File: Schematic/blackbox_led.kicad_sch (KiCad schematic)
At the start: 26 parts, among them U10 CSNP1GCR01-BOW

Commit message: reviewing and refactoring footprints and full schematic
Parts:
- C45: MPN (none) -> 0603B104K500NT; Manufacturer (none) -> FH
- C46: MPN (none) -> CC0603KRX7R9BB103; Manufacturer (none) -> YAGEO
- D10, D11, D12, D13, D3, D4, D5, D6, D7, D8, D9: MPN (none) -> NCD0603R3; Manufacturer (none) -> NATIONSTAR
- R28, R29, R30: MPN (none) -> 0603WAF4700T5E; Manufacturer (none) -> UNI-ROYAL
- R31, R32, R33, R34: MPN (none) -> RC0603FR-071KL; Manufacturer (none) -> YAGEO
- R35, R36, R37, R38, R39: MPN (none) -> 0603WAF1002T5E; Manufacturer (none) -> UNI-ROYAL
- U10: MPN (none) -> CSNP1GCR01-BOW; Manufacturer (none) -> CS Semiconductor

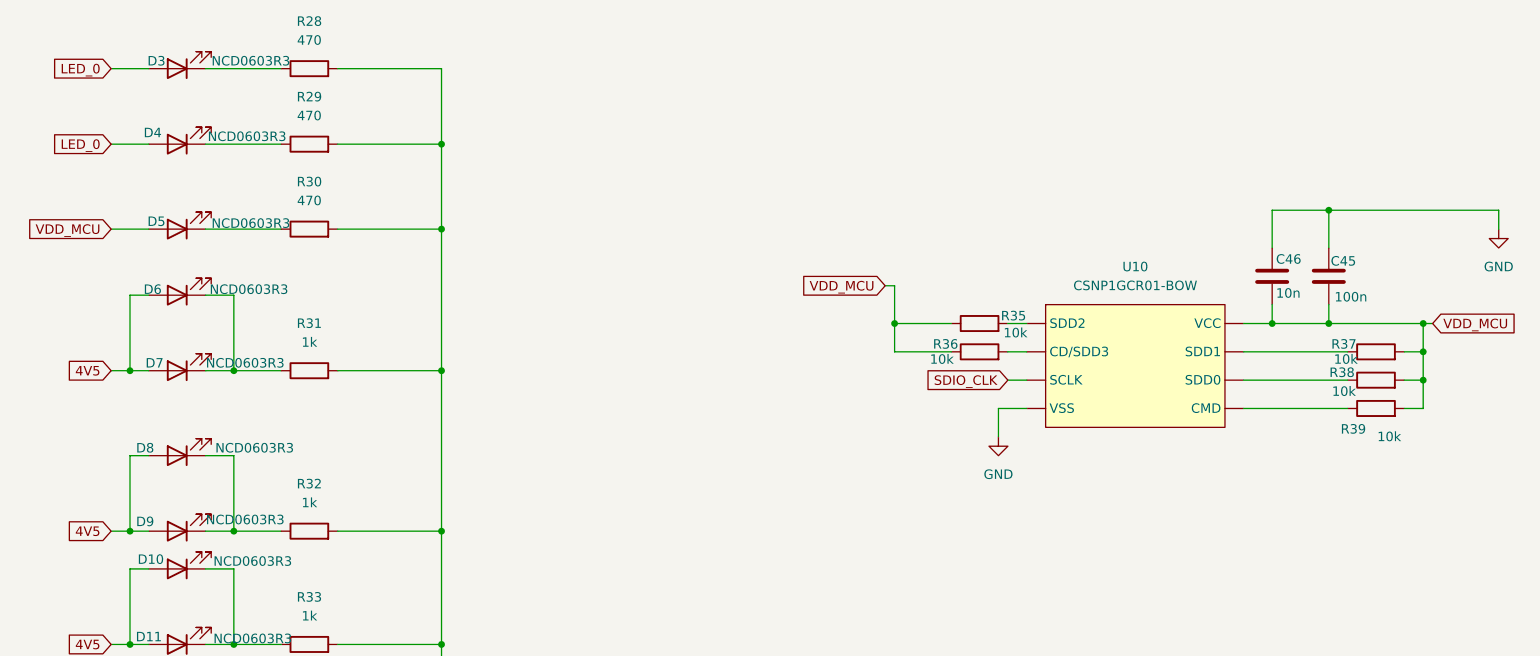
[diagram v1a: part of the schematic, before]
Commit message: Refactor fp-lib-table: Remove unused libraries and update description for fch7_fp
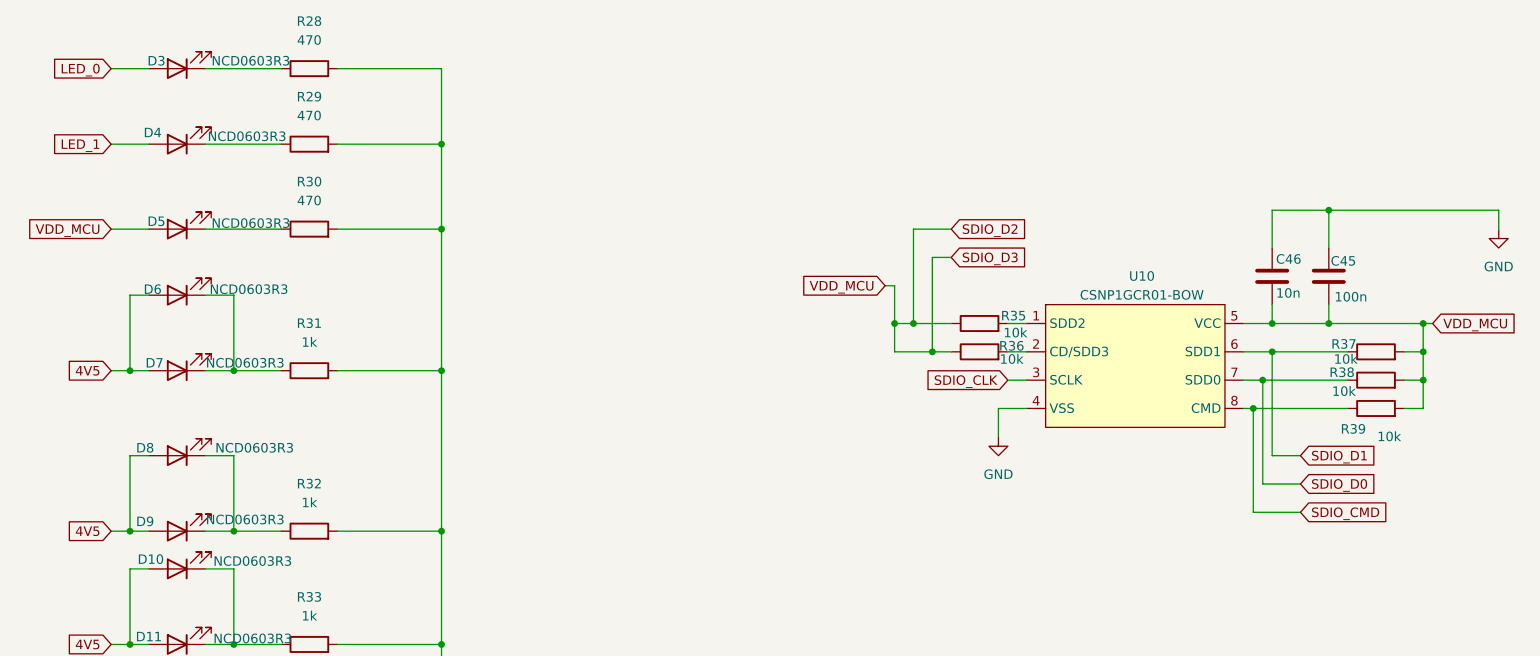
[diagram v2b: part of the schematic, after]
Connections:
- net GND: now also U10.4 (VSS); no longer U10. (CMD)
- net LED_0: no longer D4.2 (A)
- net SDIO_CLK: now also U10.3 (SCLK); no longer U10. (CMD)
- net SDIO_D0: now reaches R38.1
- net SDIO_D0: now also U10.7 (SDD0); no longer U10. (CMD)
- net SDIO_D1: now reaches R37.1
- net SDIO_D1: now also U10.6 (SDD1); no longer U10. (CMD)
- net at R35.2: now also U10.1 (SDD2); no longer U10. (CMD)
- net at R36.2: now also U10.2 (CD/SDD3); no longer U10. (CMD)
- net SDIO_CMD: now reaches R39.1
- net SDIO_CMD: now also U10.8 (CMD); no longer U10. (CMD)
- net VDD_MCU renamed SDIO_D2
- net SDIO_D2: now also U10.5 (VCC); no longer U10. (CMD)
- new net LED_1: D4.2 (A)

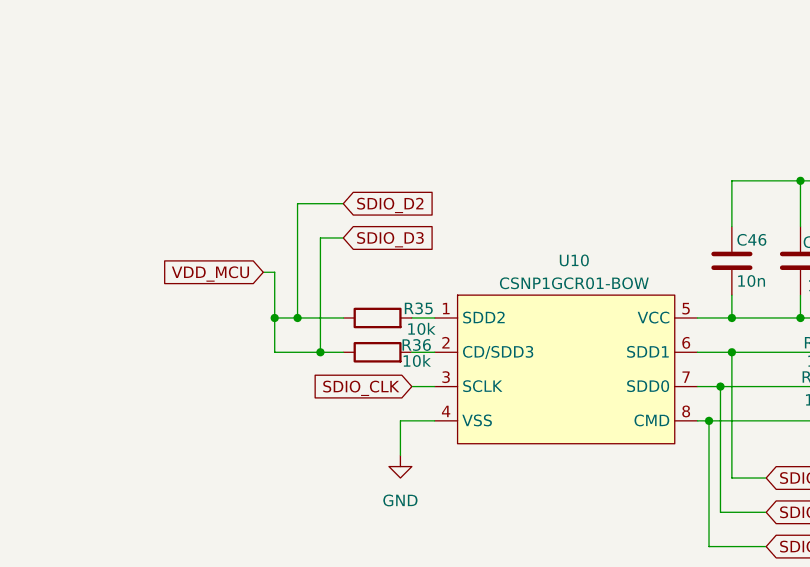
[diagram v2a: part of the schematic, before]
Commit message: Refactor schematic files and update component placements
- Adjusted component positions in osd.kicad_sch for better layout.
- Added new junctions and wires in rf_rx.kicad_sch to improve connectivity.
- Introduced additional junctions and wires in sensors.kicad_sch for enhanced signal routing.
- Removed outdated backup file fch7-2025-11-18_191836.zip and added new backup fch7-2025-11-27_202230.zip.
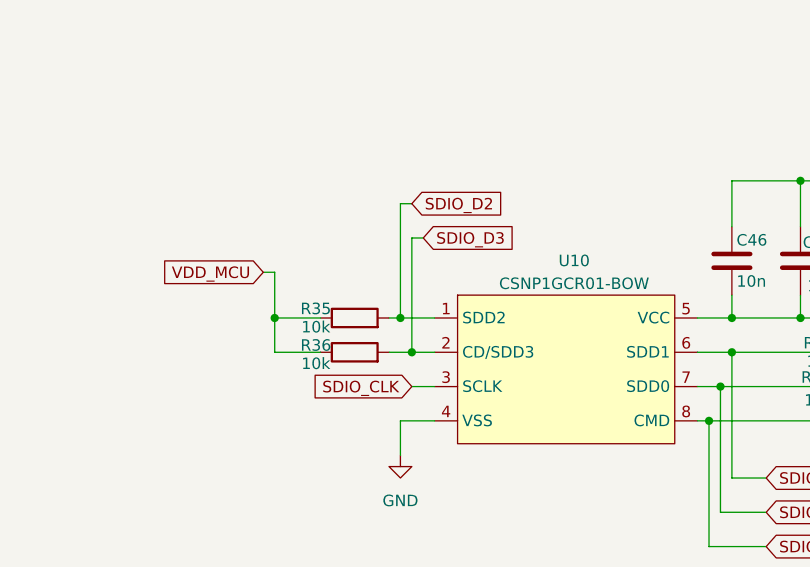
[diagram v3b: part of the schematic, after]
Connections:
- net SDIO_D2: now also R35.2, U10.1 (SDD2); no longer C45.2, C46.2, D5.2 (A), R35.1, R36.1, R37.2, R38.2, R39.2, U10.5 (VCC)
- net SDIO_D3: now reaches R36.2, U10.2 (CD/SDD3)
- new net VDD_MCU: C45.2, C46.2, D5.2 (A), R35.1, R36.1, R37.2, R38.2, R39.2, U10.5 (VCC)
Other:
- moved on the sheet: R35, R36

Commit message: Refactor code structure for improved readability and maintainability
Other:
- note added: "State LEDS indicator"
- moved on the sheet: C45, C46, D10, D11, D12, D13, D3, D4, D5, D6, D7, D8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
